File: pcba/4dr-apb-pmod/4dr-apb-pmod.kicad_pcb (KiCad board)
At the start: 2 copper layers, 198.1 x 20.3 mm, 59 parts

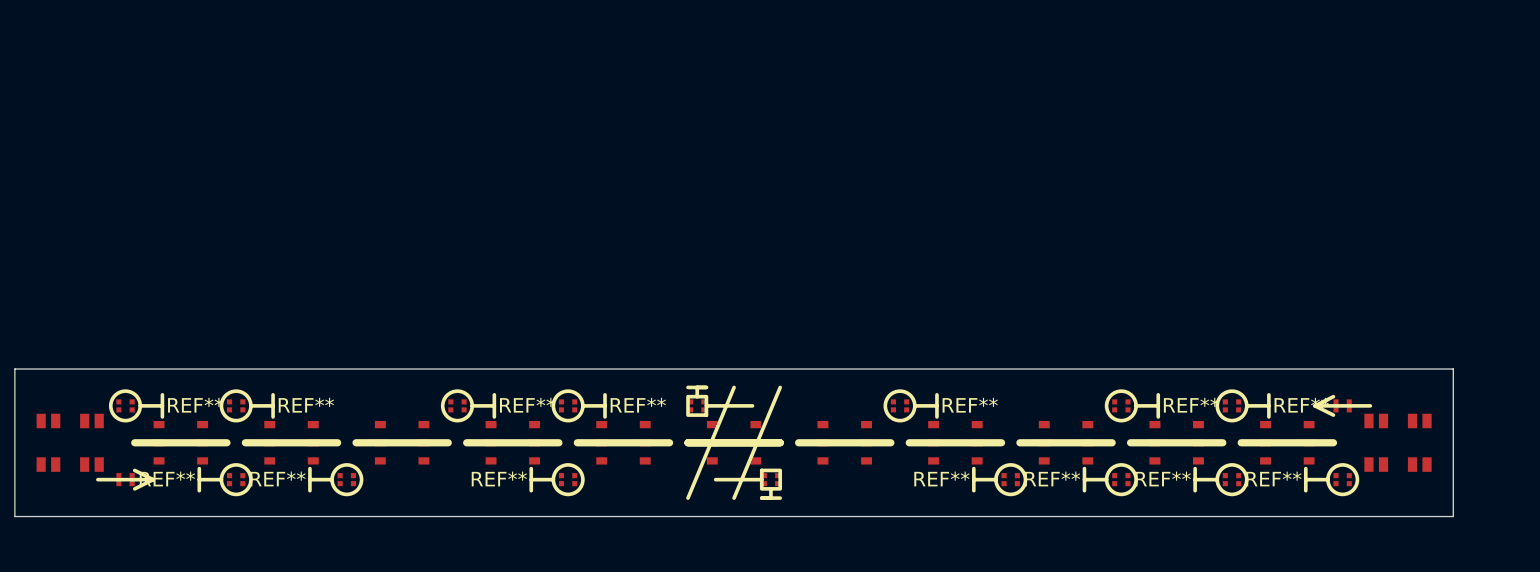
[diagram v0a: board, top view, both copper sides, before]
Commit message: Add schematic and 3D models
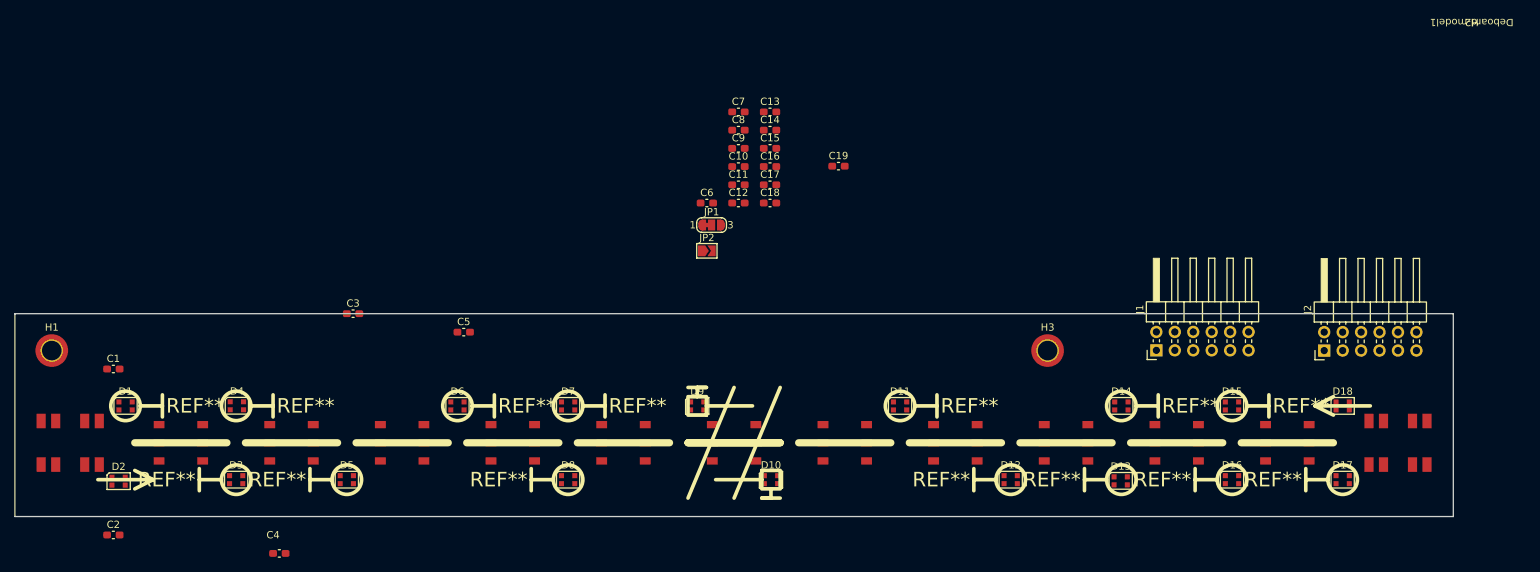
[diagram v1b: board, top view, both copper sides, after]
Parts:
- removed the REF** at (68.6, 106.7)
- removed the REF** at (114.3, 96.5)
- removed the REF** at (68.6, 96.5)
- removed the REF** at (83.8, 96.5)
- removed the REF** at (157.5, 106.7)
- removed the REF** at (190.5, 106.7)
- removed the REF** at (129.5, 96.5)
- removed the REF** at (99.1, 106.7)
- removed the REF** at (236.2, 106.7)
- removed the REF** at (175.3, 96.5)
- removed the REF** at (129.5, 106.7)
- removed the REF** at (205.7, 96.5)
- removed the REF** at (221.0, 106.7)
- removed the REF** at (221.0, 96.5)
- removed the REF** at (236.2, 96.5)
- removed the REF** at (205.7, 106.7)
- removed the REF** at (83.8, 106.7)
- removed the REF** at (147.3, 96.5)
- added C1: 0.1u, Capacitor_SMD:C_0603_1608Metric_Pad1.08x0.95mm_HandSolder, F.Cu at (66.9, 91.4)
- added C10: 0.1u, Capacitor_SMD:C_0603_1608Metric_Pad1.08x0.95mm_HandSolder, F.Cu at (153.0, 63.6)
- added C11: 0.1u, Capacitor_SMD:C_0603_1608Metric_Pad1.08x0.95mm_HandSolder, F.Cu at (153.0, 66.1)
- added C12: 0.1u, Capacitor_SMD:C_0603_1608Metric_Pad1.08x0.95mm_HandSolder, F.Cu at (153.0, 68.6)
- added C13: 0.1u, Capacitor_SMD:C_0603_1608Metric_Pad1.08x0.95mm_HandSolder, F.Cu at (157.3, 56.0)
- added C14: 0.1u, Capacitor_SMD:C_0603_1608Metric_Pad1.08x0.95mm_HandSolder, F.Cu at (157.3, 58.5)
- added C15: 0.1u, Capacitor_SMD:C_0603_1608Metric_Pad1.08x0.95mm_HandSolder, F.Cu at (157.3, 61.0)
- added C16: 0.1u, Capacitor_SMD:C_0603_1608Metric_Pad1.08x0.95mm_HandSolder, F.Cu at (157.3, 63.6)
- added C17: 0.1u, Capacitor_SMD:C_0603_1608Metric_Pad1.08x0.95mm_HandSolder, F.Cu at (157.3, 66.1)
- added C18: 0.1u, Capacitor_SMD:C_0603_1608Metric_Pad1.08x0.95mm_HandSolder, F.Cu at (157.3, 68.6)
- added C19: 0.1u, Capacitor_SMD:C_0603_1608Metric_Pad1.08x0.95mm_HandSolder, F.Cu at (166.8, 63.5)
- added C2: 0.1u, Capacitor_SMD:C_0603_1608Metric_Pad1.08x0.95mm_HandSolder, F.Cu at (66.9, 114.3)
- added C3: 0.1u, Capacitor_SMD:C_0603_1608Metric_Pad1.08x0.95mm_HandSolder, F.Cu at (99.9, 83.8)
- added C4: 0.1u, Capacitor_SMD:C_0603_1608Metric_Pad1.08x0.95mm_HandSolder, F.Cu at (89.8, 116.8)
- added C5: 0.1u, Capacitor_SMD:C_0603_1608Metric_Pad1.08x0.95mm_HandSolder, F.Cu at (115.2, 86.4)
- added C6: 0.1u, Capacitor_SMD:C_0603_1608Metric_Pad1.08x0.95mm_HandSolder, F.Cu at (148.6, 68.6)
- added C7: 0.1u, Capacitor_SMD:C_0603_1608Metric_Pad1.08x0.95mm_HandSolder, F.Cu at (153.0, 56.0)
- added C8: 0.1u, Capacitor_SMD:C_0603_1608Metric_Pad1.08x0.95mm_HandSolder, F.Cu at (153.0, 58.5)
- added C9: 0.1u, Capacitor_SMD:C_0603_1608Metric_Pad1.08x0.95mm_HandSolder, F.Cu at (153.0, 61.0)
- added D1: WS2812B-2020, LED_SMD:LED_WS2812B-2020_PLCC4_2.0x2.0mm, F.Cu at (68.6, 96.5)
- added D10: WS2812B-2020, LED_SMD:LED_WS2812B-2020_PLCC4_2.0x2.0mm, F.Cu at (157.5, 106.7)
- added D11: WS2812B-2020, LED_SMD:LED_WS2812B-2020_PLCC4_2.0x2.0mm, F.Cu at (175.3, 96.5)
- added D12: WS2812B-2020, LED_SMD:LED_WS2812B-2020_PLCC4_2.0x2.0mm, F.Cu at (190.5, 106.7)
- added D13: WS2812B-2020, LED_SMD:LED_WS2812B-2020_PLCC4_2.0x2.0mm, F.Cu at (205.6, 106.8)
- added D14: WS2812B-2020, LED_SMD:LED_WS2812B-2020_PLCC4_2.0x2.0mm, F.Cu at (205.7, 96.5)
- added D15: WS2812B-2020, LED_SMD:LED_WS2812B-2020_PLCC4_2.0x2.0mm, F.Cu at (221.0, 96.5)
- added D16: WS2812B-2020, LED_SMD:LED_WS2812B-2020_PLCC4_2.0x2.0mm, F.Cu at (221.0, 106.7)
- added D17: WS2812B-2020, LED_SMD:LED_WS2812B-2020_PLCC4_2.0x2.0mm, F.Cu at (236.2, 106.7)
- added D18: WS2812B-2020, LED_SMD:LED_WS2812B-2020_PLCC4_2.0x2.0mm, F.Cu at (236.2, 96.5)
- added D2: WS2812B-2020, LED_SMD:LED_WS2812B-2020_PLCC4_2.0x2.0mm, F.Cu at (67.6, 106.9)
- added D3: WS2812B-2020, LED_SMD:LED_WS2812B-2020_PLCC4_2.0x2.0mm, F.Cu at (83.8, 106.7)
- added D4: WS2812B-2020, LED_SMD:LED_WS2812B-2020_PLCC4_2.0x2.0mm, F.Cu at (83.9, 96.5)
- added D5: WS2812B-2020, LED_SMD:LED_WS2812B-2020_PLCC4_2.0x2.0mm, F.Cu at (99.1, 106.7)
- added D6: WS2812B-2020, LED_SMD:LED_WS2812B-2020_PLCC4_2.0x2.0mm, F.Cu at (114.3, 96.5)
- added D7: WS2812B-2020, LED_SMD:LED_WS2812B-2020_PLCC4_2.0x2.0mm, F.Cu at (129.5, 96.5)
- added D8: WS2812B-2020, LED_SMD:LED_WS2812B-2020_PLCC4_2.0x2.0mm, F.Cu at (129.5, 106.7)
- added D9: WS2812B-2020, LED_SMD:LED_WS2812B-2020_PLCC4_2.0x2.0mm, F.Cu at (147.3, 96.5)
- added Deboard-model1, H2: MountingHole_Pad, 4dr-apb-mod:icebreaker_dev, F.Cu at (254.0, 43.2)
- added H1: MountingHole_Pad, MountingHole:MountingHole_2.7mm_M2.5_ISO7380_Pad_TopOnly, F.Cu at (58.4, 88.9)
- added H3: MountingHole_Pad, MountingHole:MountingHole_2.7mm_M2.5_ISO7380_Pad_TopOnly, F.Cu at (195.6, 88.9)
- added J1: Conn_02x06_Row_Letter_Last, Connector_PinHeader_2.54mm:PinHeader_2x06_P2.54mm_Horizontal, F.Cu at (210.6, 88.9)
- added J2: Conn_02x06_Row_Letter_Last, Connector_PinHeader_2.54mm:PinHeader_2x06_P2.54mm_Horizontal, F.Cu at (233.7, 88.9)
- added JP1: SolderJumper_3_Bridged12, Jumper:SolderJumper-3_P1.3mm_Bridged12_RoundedPad1.0x1.5mm_NumberLabels, F.Cu at (149.3, 71.6)
- added JP2: SolderJumper_2_Open, Jumper:SolderJumper-2_P1.3mm_Open_TrianglePad1.0x1.5mm, F.Cu at (148.6, 75.2)
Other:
- board size 198.1 x 20.3 mm -> 198.1 x 27.9 mm
- board text added: "${REFERENCE}"
